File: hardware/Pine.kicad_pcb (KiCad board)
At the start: 2 copper layers, 45.7 x 38.1 mm, 51 parts, among them J1 USB Micro type-B, J2 01x06 Male conn, J3 Battery connector, Q1 p-channel MOSFET, Q2 NPN Transistor, SW1 Switch, SW2 Push button, U1 IR Receiver, U2 LDO, U3 Temperature sensor, U4 MCU

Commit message: feat: improve routing
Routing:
- net Net-(TP4-Pad1): track 45.1 -> 46.0 mm

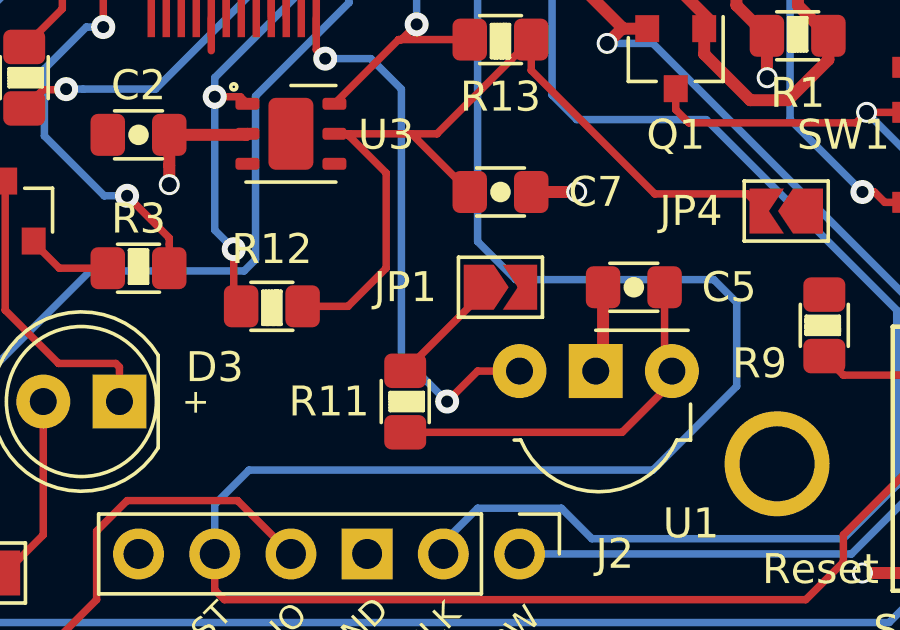
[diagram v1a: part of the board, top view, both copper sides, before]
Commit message: fix: remove redundant solder jumper. #14
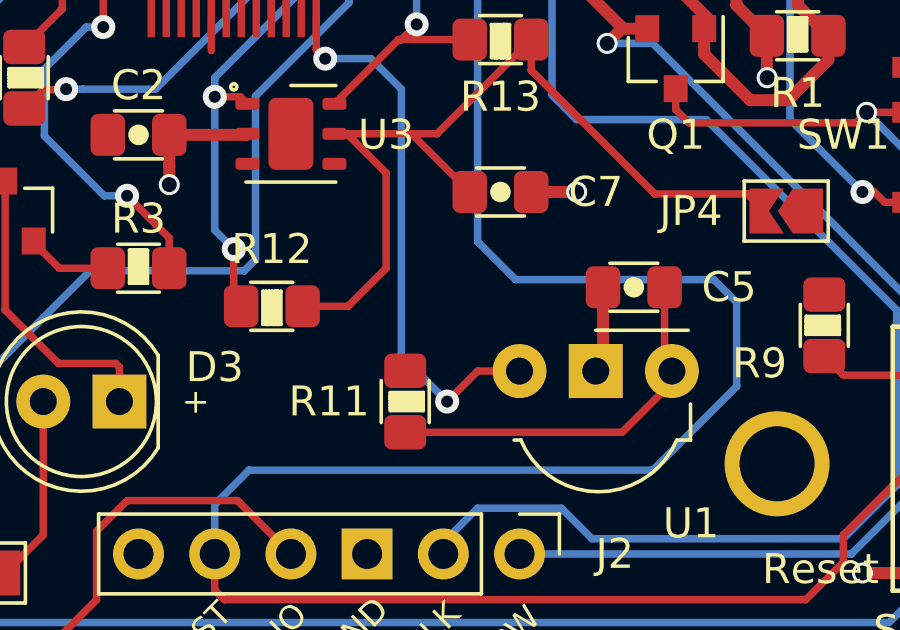
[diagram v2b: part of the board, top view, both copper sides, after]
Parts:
- removed JP1: Open solder jumper, Jumper:SolderJumper-2_P1.3mm_Open_TrianglePad1.0x1.5mm
- removed REF**: OSHW-Logo2_9.8x8mm_SilkScreen, Symbol:OSHW-Logo2_9.8x8mm_SilkScreen
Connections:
- R11 pad 1: Net-(JP1-Pad1) -> /2V8
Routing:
- net Net-(JP1-Pad1): track 3.80 -> 0.00 mm

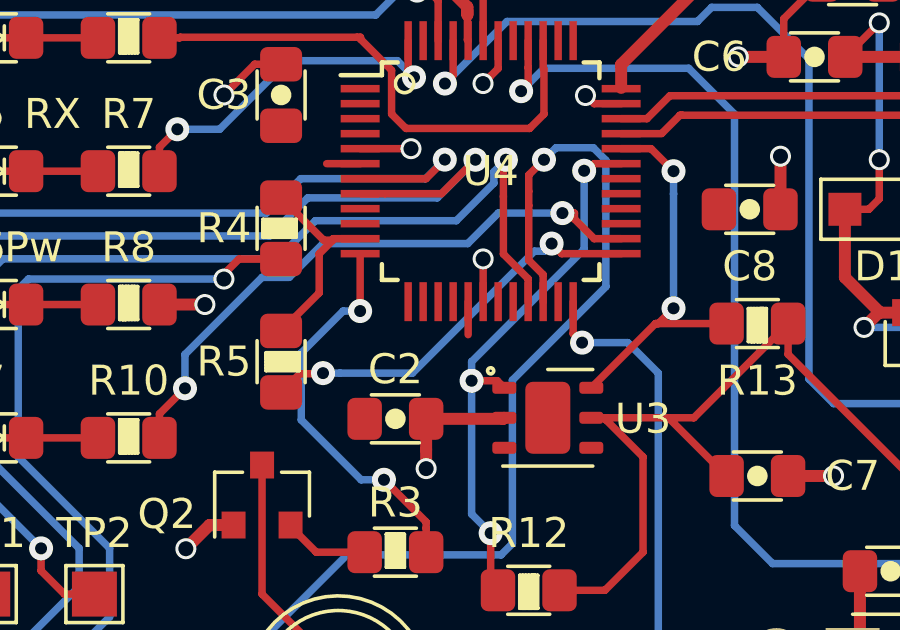
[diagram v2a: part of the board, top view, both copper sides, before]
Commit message: fix: remove BATT_EN and link to GND. #14
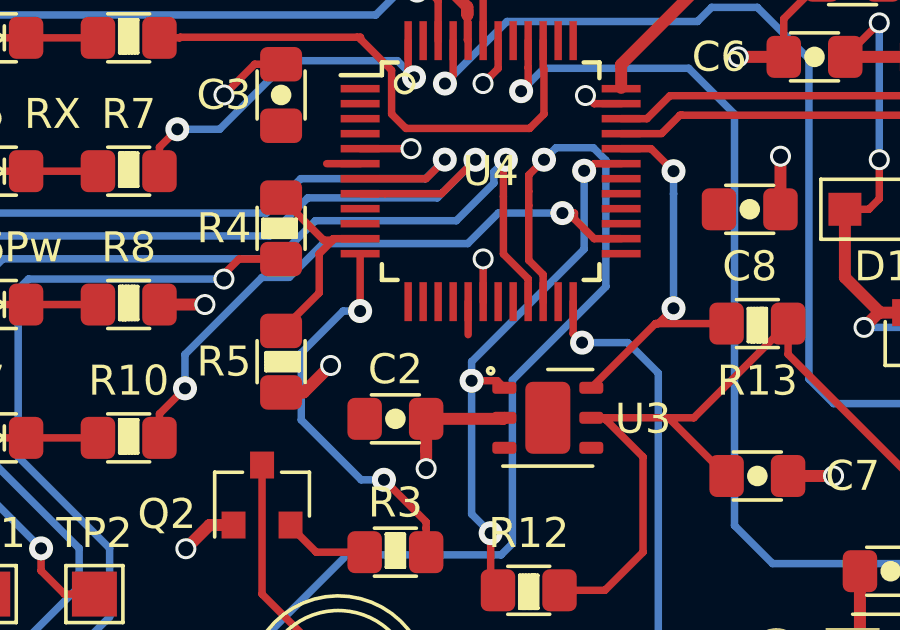
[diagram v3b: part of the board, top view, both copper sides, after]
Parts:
- added REF**: OSHW-Logo2_9.8x8mm_SilkScreen, Symbol:OSHW-Logo2_9.8x8mm_SilkScreen, B.Cu at (176.5, 59.1)
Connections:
- R5 pad 2: /Batt_EN -> GND
- U4 pad 25: /Batt_EN -> (no net)
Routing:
- net /Batt_EN: track 13.5 -> 0.00 mm, vias 2 -> 0
- net GND: track 48.7 -> 50.8 mm, vias 19 -> 20

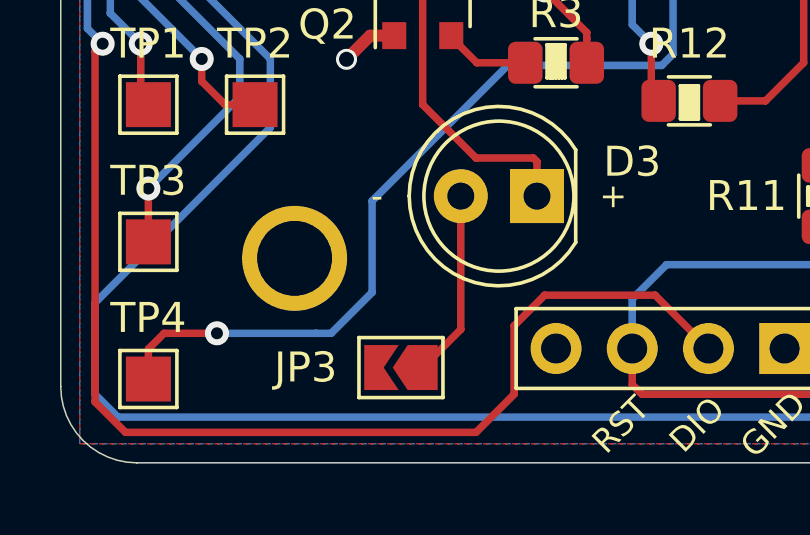
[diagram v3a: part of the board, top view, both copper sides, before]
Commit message: fix: add series resistor to IR LED. #14
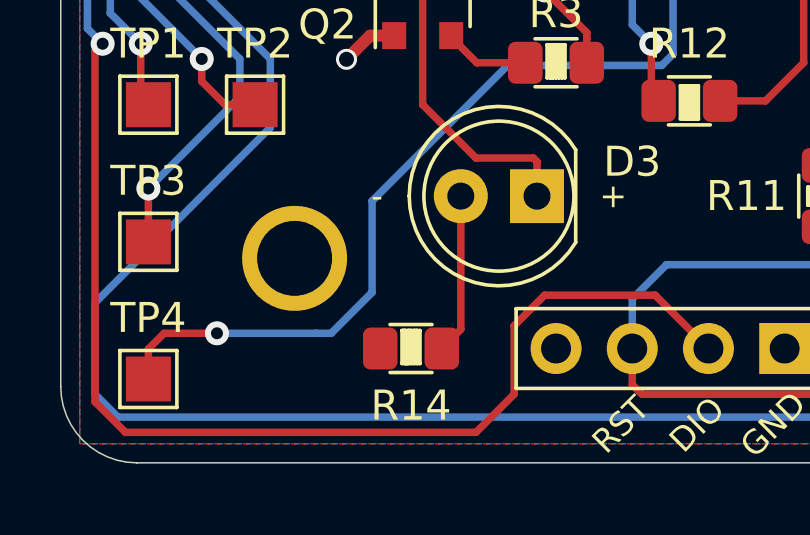
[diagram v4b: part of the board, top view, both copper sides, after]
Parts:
- removed JP3: Open solder jumper, Jumper:SolderJumper-2_P1.3mm_Open_TrianglePad1.0x1.5mm
- added R14: 0R, Passives_0805:R_0805_2012Metric_Pad1.15x1.40mm_HandSolder, F.Cu at (164.7, 76.2)
- moved REF** 0.63 mm to (175.9, 59.1)
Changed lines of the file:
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@@
   )
   (module Symbol:OSHW-Logo2_9.8x8mm_SilkScreen (layer B.Cu)
-    (at 176.53 59.055 180)
+    (at 175.895 59.055 180)
     (descr "Open Source Hardware Symbol")
     (tags "Logo Symbol OSHW")
@@
       (xy -3.43224 -2.584467) (xy -3.324904 -2.572722) (xy -3.231114 -2.584505)) (layer B.SilkS) (width 0.01))
   )
+  (module Passives_0805:R_0805_2012Metric_Pad1.15x1.40mm_HandSolder (layer F.Cu)
+    (at 164.71 76.2)
+    (descr "Resistor SMD 0805 (2012 Metric), square (rectangular) end terminal, IPC_7351 nominal with elongated pad for handsoldering. (Body size source: https://docs.google.com/spreadsheets/d/1BsfQQcO9C6DZCsRaXUlFlo91Tg2WpOkGARC1WS5S8t0/edit?usp=sharing), generated with kicad-footprint-generator")
+    (tags "resistor handsolder")
+    (attr smd)
+    (fp_text reference R14 (at 0 1.905) (layer F.SilkS)
+      (effects (font (size 1 1) (thickness 0.15)))
+    )
+    (fp_text value 0R (at 0 1.65) (layer F.Fab)
+      (effects (font (size 1 1) (thickness 0.15)))
+    )
+    (fp_line (start 0.1 -0.6) (end 0.1 0.5) (layer F.SilkS) (width 0.12))
+    (fp_line (start 0.2 -0.6) (end 0.1 -0.6) (layer F.SilkS) (width 0.12))
+    (fp_line (start 0.2 0.5) (end 0.2 -0.6) (layer F.SilkS) (width 0.12))
+    (fp_line (start 0 -0.6) (end 0 0.5) (layer F.SilkS) (width 0.12))
+    (fp_line (start -0.1 -0.6) (end 0 -0.6) (layer F.SilkS) (width 0.12))
+    (fp_line (start -0.1 0.5) (end -0.1 -0.6) (layer F.SilkS) (width 0.12))
+    (fp_line (start -0.2 0.5) (end -0.1 0.5) (layer F.SilkS) (width 0.12))
+    (fp_line (start -0.2 0.4) (end -0.2 0.5) (layer F.SilkS) (width 0.12))
+    (fp_line (start -0.2 -0.6) (end -0.2 0.4) (layer F.SilkS) (width 0.12))
+    (fp_line (start -0.3 -0.6) (end -0.2 -0.6) (layer F.SilkS) (width 0.12))
+    (fp_line (start -0.2 -0.6) (end -0.3 -0.6) (layer F.SilkS) (width 0.12))
+    (fp_line (start 0.3 -0.6) (end -0.2 -0.6) (layer F.SilkS) (width 0.12))
+    (fp_line (start 0.3 0.5) (end 0.3 -0.6) (layer F.SilkS) (width 0.12))
+    (fp_line (start -0.3 0.5) (end 0.3 0.5) (layer F.SilkS) (width 0.12))
+    (fp_line (start -0.3 -0.6) (end -0.3 0.5) (layer F.SilkS) (width 0.12))
+    (fp_line (start -0.7 0.8) (end 0.7 0.8) (layer F.SilkS) (width 0.12))
+    (fp_line (start -0.7 -0.8) (end 0.7 -0.8) (layer F.SilkS) (width 0.12))
+    (fp_text user %R (at 0 0) (layer F.Fab)
+      (effects (font (size 0.5 0.5) (thickness 0.08)))
+    )
+    (fp_line (start 1.85 0.95) (end -1.85 0.95) (layer F.CrtYd) (width 0.05))
+    (fp_line (start 1.85 -0.95) (end 1.85 0.95) (layer F.CrtYd) (width 0.05))
+    (fp_line (start -1.85 -0.95) (end 1.85 -0.95) (layer F.CrtYd) (width 0.05))
+    (fp_line (start -1.85 0.95) (end -1.85 -0.95) (layer F.CrtYd) (width 0.05))
+    (fp_line (start 1 0.6) (end -1 0.6) (layer F.Fab) (width 0.1))
+    (fp_line (start 1 -0.6) (end 1 0.6) (layer F.Fab) (width 0.1))
+    (fp_line (start -1 -0.6) (end 1 -0.6) (layer F.Fab) (width 0.1))
+    (fp_line (start -1 0.6) (end -1 -0.6) (layer F.Fab) (width 0.1))
+    (pad 2 smd roundrect (at 1.025 0) (size 1.15 1.4) (layers F.Cu F.Paste F.Mask) (roundrect_rratio 0.217391)
+      (net 8 "Net-(D3-Pad2)"))
+    (pad 1 smd roundrect (at -1.025 0) (size 1.15 1.4) (layers F.Cu F.Paste F.Mask) (roundrect_rratio 0.217391)
+      (net 2 /2V8))
+    (model ${KISYS3DMOD}/Resistor_SMD.3dshapes/R_0805_2012Metric.wrl
+      (at (xyz 0 0 0))
+      (scale (xyz 1 1 1))
+      (rotate (xyz 0 0 0))
+    )
+  )
   (module LED_THT:LED_D5.0mm_IRGrey (layer F.Cu)
     (at 168.91 71.12 180)
@@
     (pad 2 smd custom (at 0.725 0 180) (size 0.3 0.3) (layers F.Cu F.Mask)
       (net 5 "Net-(C7-Pad1)") (zone_connect 2)
-      (options (clearance outline) (anchor rect))
-      (primitives
-        (gr_poly (pts
-           (xy -0.65 -0.75) (xy 0.5 -0.75) (xy 0.5 0.75) (xy -0.65 0.75) (xy -0.15 0)
-) (width 0))
-      ))
-  )
-  (module Jumper:SolderJumper-2_P1.3mm_Open_TrianglePad1.0x1.5mm (layer F.Cu)
-    (at 164.375 76.835 180)
-    (descr "SMD Solder Jumper, 1x1.5mm Triangular Pads, 0.3mm gap, open")
-    (tags "solder jumper open")
-    (attr virtual)
-    (fp_text reference JP3 (at 3.175 0 180) (layer F.SilkS)
-      (effects (font (size 1 1) (thickness 0.15)))
-    )
-    (fp_text value "Open solder jumper" (at 0 1.9 180) (layer F.Fab)
-      (effects (font (size 1 1) (thickness 0.15)))
-    )
-    (fp_line (start 1.65 1.25) (end -1.65 1.25) (layer F.CrtYd) (width 0.05))
-    (fp_line (start 1.65 1.25) (end 1.65 -1.25) (layer F.CrtYd) (width 0.05))
-    (fp_line (start -1.65 -1.25) (end -1.65 1.25) (layer F.CrtYd) (width 0.05))
-    (fp_line (start -1.65 -1.25) (end 1.65 -1.25) (layer F.CrtYd) (width 0.05))
-    (fp_line (start -1.4 -1) (end 1.4 -1) (layer F.SilkS) (width 0.12))
-    (fp_line (start 1.4 -1) (end 1.4 1) (layer F.SilkS) (width 0.12))
-    (fp_line (start 1.4 1) (end -1.4 1) (layer F.SilkS) (width 0.12))
-    (fp_line (start -1.4 1) (end -1.4 -1) (layer F.SilkS) (width 0.12))
-    (pad 1 smd custom (at -0.725 0 180) (size 0.3 0.3) (layers F.Cu F.Mask)
-      (net 8 "Net-(D3-Pad2)") (zone_connect 2)
-      (options (clearance outline) (anchor rect))
-      (primitives
-        (gr_poly (pts
-           (xy -0.5 -0.75) (xy 0.5 -0.75) (xy 1 0) (xy 0.5 0.75) (xy -0.5 0.75)
-) (width 0))
-      ))
-    (pad 2 smd custom (at 0.725 0 180) (size 0.3 0.3) (layers F.Cu F.Mask)
-      (net 2 /2V8) (zone_connect 2)
       (options (clearance outline) (anchor rect))
       (primitives
@@
   (segment (start 185.51 47.325) (end 185.81 47.625) (width 0.25) (layer F.Cu) (net 7))
   (segment (start 185.51 44.45) (end 185.51 47.325) (width 0.25) (layer F.Cu) (net 7))
-  (segment (start 166.37 75.565) (end 165.1 76.835) (width 0.25) (layer F.Cu) (net 8))
-  (segment (start 166.37 71.755) (end 166.37 75.565) (width 0.25) (layer F.Cu) (net 8))
+  (segment (start 166.37 75.565) (end 165.735 76.2) (width 0.25) (layer F.Cu) (net 8))
+  (segment (start 166.37 71.12) (end 166.37 75.565) (width 0.25) (layer F.Cu) (net 8))
   (segment (start 168.91 69.97) (end 168.91 71.12) (width 0.25) (layer F.Cu) (net 9))
   (segment (start 166.878 69.85) (end 168.79 69.85) (width 0.25) (layer F.Cu) (net 9))

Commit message: chore: update all assets before manufacturing
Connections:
- net /2V8 renamed +2V8
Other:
- board text added: "Pine@Hutscape V1.0 Nov 2019"
- board text removed: "Pine@Hutscape V1.0 2019"
